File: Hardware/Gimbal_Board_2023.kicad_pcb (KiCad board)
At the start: 2 copper layers, 139 x 93.5 mm, 72 parts, among them J1 6P6C, J2 RJ45_LED_Shielded, Q1 Q_NMOS_GDS, Q2 Q_NMOS_GDS, Q3 Q_NMOS_GDS, Q4 Q_NMOS_GDS, Q5 Q_NMOS_GDS, Q6 Q_NMOS_GDS, Q7 Q_NMOS_GDS, SW1 SW_Push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

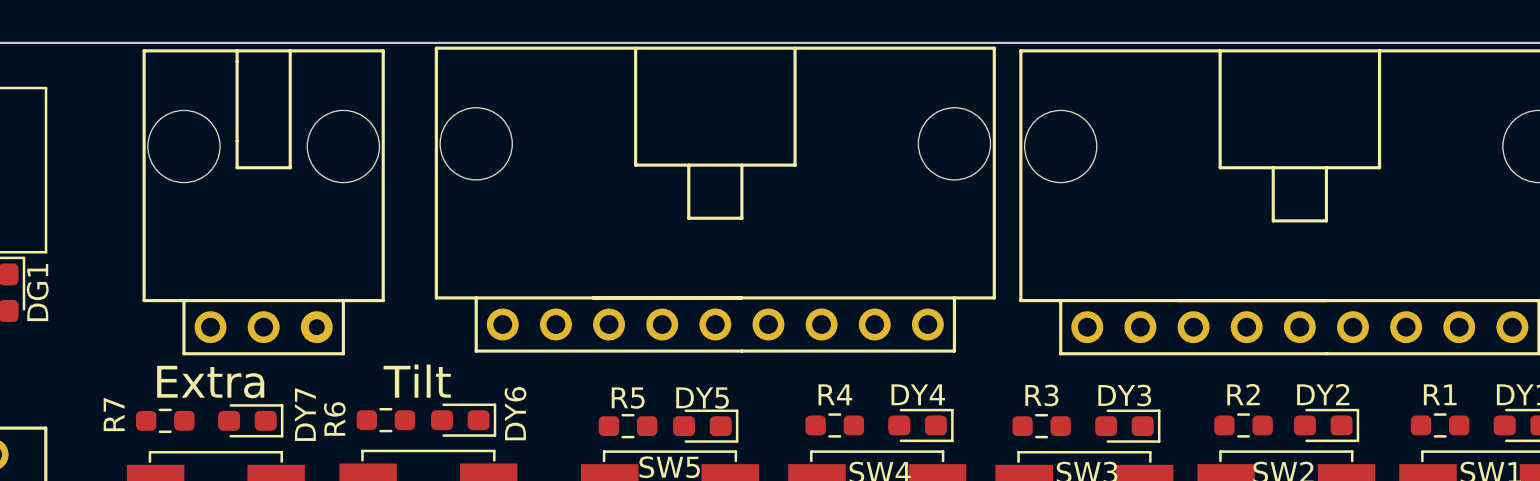
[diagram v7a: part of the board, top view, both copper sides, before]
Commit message: Started servo port 5v
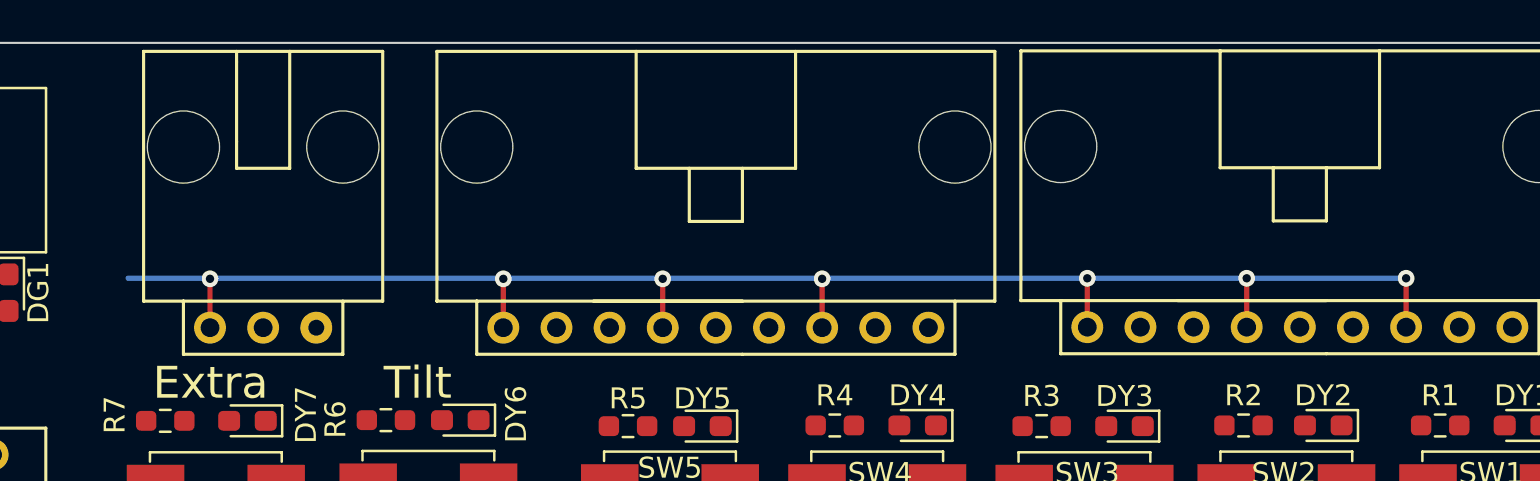
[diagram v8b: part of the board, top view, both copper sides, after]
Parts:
- moved Conn7 0.15 mm to (124.7, 49.4)
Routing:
- net +5V: track 0.18 -> 77.6 mm, vias 0 -> 7
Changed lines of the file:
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@@
   )
   (footprint "MRDT_Connectors:MOLEX_SL_03_Horizontal" (layer "F.Cu")
-    (at 110.744 49.403)
+    (at 110.7186 49.4284)
     (property "Sheetfile" "Gimbal_Board_2023.kicad_sch")
     (property "Sheetname" "")
@@
   )
   (footprint "MRDT_Connectors:MOLEX_SL_09_Horizontal" (layer "F.Cu")
-    (at 124.714 49.276)
+    (at 124.7394 49.4284)
     (property "Sheetfile" "Gimbal_Board_2023.kicad_sch")
     (property "Sheetname" "")
@@
   (segment (start 146.266 64.496) (end 146.064 64.294) (width 0.25) (layer "F.Cu") (net 38))
   (segment (start 149.8165 60.513) (end 148.3535 60.513) (width 0.25) (layer "F.Cu") (net 45))
+  (segment (start 152.654 49.403) (end 152.654 47.0662) (width 0.254) (layer "F.Cu") (net 59))
+  (segment (start 139.9794 49.4284) (end 139.9794 47.0916) (width 0.254) (layer "F.Cu") (net 59))
+  (segment (start 160.274 49.403) (end 160.274 47.0662) (width 0.254) (layer "F.Cu") (net 59))
+  (segment (start 124.7394 49.4284) (end 124.7394 47.0916) (width 0.254) (layer "F.Cu") (net 59))
+  (segment (start 167.894 49.403) (end 167.894 47.0662) (width 0.254) (layer "F.Cu") (net 59))
+  (segment (start 110.7186 49.4284) (end 110.7186 47.0916) (width 0.254) (layer "F.Cu") (net 59))
+  (segment (start 132.3594 49.4284) (end 132.3594 47.0916) (width 0.254) (layer "F.Cu") (net 59))
   (segment (start 99.441 46.703) (end 99.314 46.83) (width 0.25) (layer "F.Cu") (net 59))
+  (via (at 110.7186 47.0916) (size 0.8) (drill 0.4) (layers "F.Cu" "B.Cu") (net 59))
+  (via (at 132.3594 47.0916) (size 0.8) (drill 0.4) (layers "F.Cu" "B.Cu") (net 59))
+  (via (at 167.894 47.0662) (size 0.8) (drill 0.4) (layers "F.Cu" "B.Cu") (net 59))
+  (via (at 152.654 47.0662) (size 0.8) (drill 0.4) (layers "F.Cu" "B.Cu") (net 59))
+  (via (at 124.7394 47.0916) (size 0.8) (drill 0.4) (layers "F.Cu" "B.Cu") (net 59))
+  (via (at 160.274 47.0662) (size 0.8) (drill 0.4) (layers "F.Cu" "B.Cu") (net 59))
+  (via (at 139.9794 47.0916) (size 0.8) (drill 0.4) (layers "F.Cu" "B.Cu") (net 59))
+  (segment (start 167.894 47.0662) (end 106.807 47.0662) (width 0.254) (layer "B.Cu") (net 59))
   (segment (start 99.31 48.659) (end 99.314 48.655) (width 0.25) (layer "F.Cu") (net 60))
 )
